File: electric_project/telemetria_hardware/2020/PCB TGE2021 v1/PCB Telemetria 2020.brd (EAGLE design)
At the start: 160 x 100 mm, 23 parts, among them IC1 INA240A1DR, IC2 MCP3221A6T-E_OTVAO, IC3 AZ1117IH-3.3TRG1, IC4 ACS758LCB-050B-PFF-T, J1 74655095R, J2 74655095R

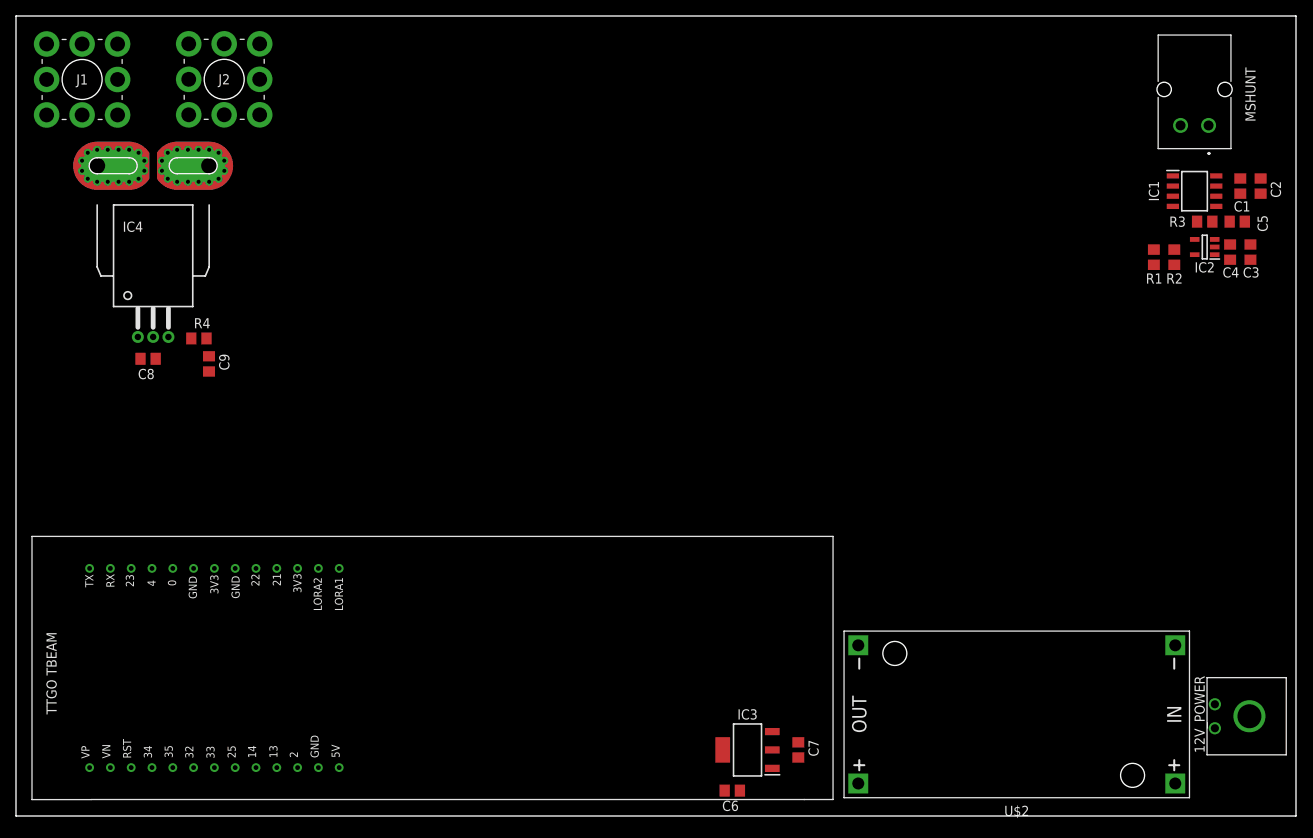
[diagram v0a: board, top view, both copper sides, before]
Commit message: Adding Current Input Traces an planes.
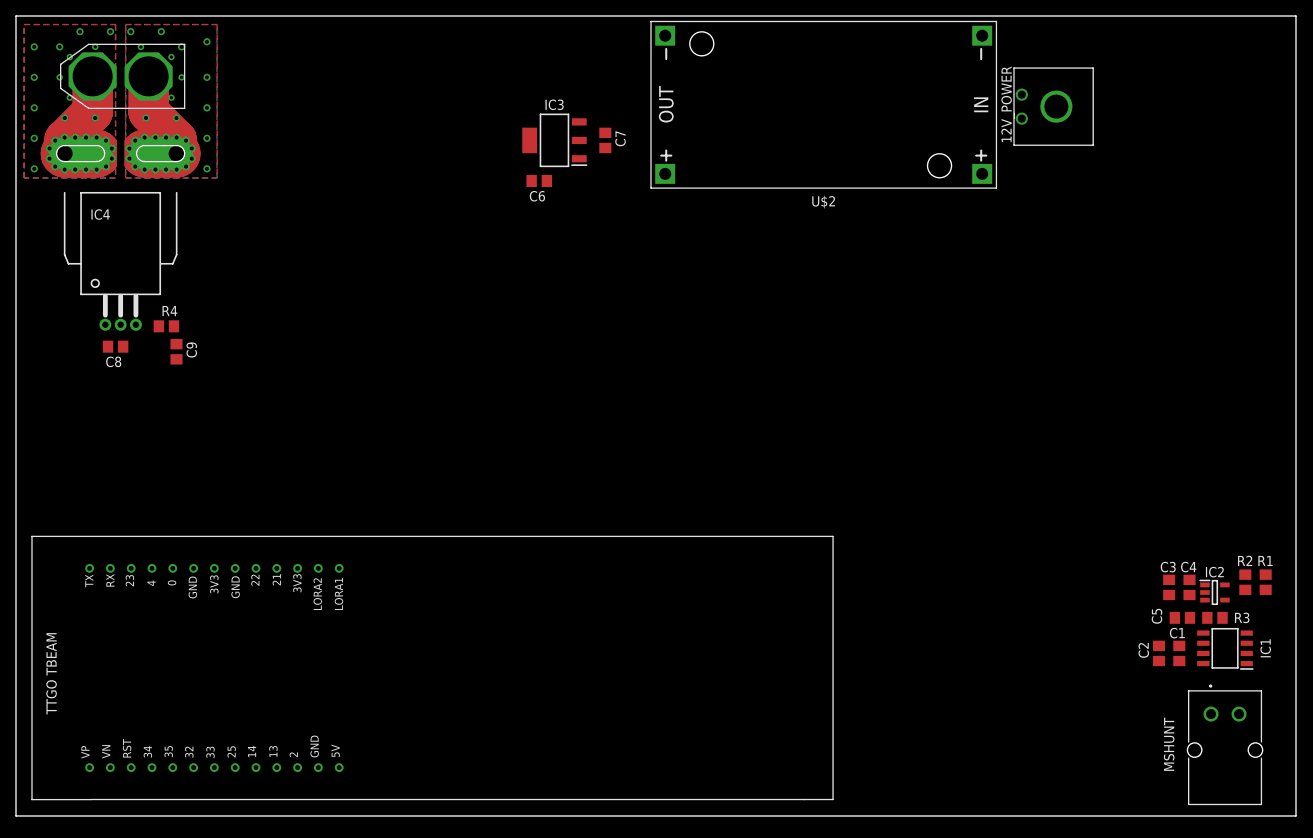
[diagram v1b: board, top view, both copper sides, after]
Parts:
- removed J1, J2: 74655095R, SamacSys_Parts:74655095R
- added U$3: XT60, XT60:XT60
- moved MSHUNT 81.4 mm to (151.1, 8.89), turned to 0 degrees
- moved 12V_POWER 79.9 mm to (125.7, 90.2)
- moved C6 79.9 mm to (65.4, 79.4)
- moved C7 79.9 mm to (73.7, 84.5)
- moved IC3 79.9 mm to (67.3, 84.5)
- moved U$2 79.9 mm to (101.0, 88.9)
- moved C2 59.8 mm to (142.9, 20.3), turned to 270 degrees
- moved C1 58.9 mm to (145.4, 20.3), turned to 270 degrees
- moved IC1 57.3 mm to (151.1, 21.0), turned to 180 degrees
- moved C5 50.0 mm to (145.8, 24.8), turned to 180 degrees
- moved R3 49.5 mm to (149.9, 24.8), turned to 0 degrees
- moved IC2 43.2 mm to (149.9, 27.9), turned to 0 degrees
- moved C3 43.1 mm to (144.1, 28.6), turned to 270 degrees
- moved R1 43.0 mm to (156.2, 29.2), turned to 90 degrees
- moved C4 42.2 mm to (146.7, 28.6), turned to 270 degrees
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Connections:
- net CMPPT_M: now also U$3.-; no longer J1.1, J1.2, J1.3, J1.4, J1.5, J1.6, J1.7, J1.8
- net CMPPT_P: now also U$3.+; no longer J2.1, J2.2, J2.3, J2.4, J2.5, J2.6, J2.7, J2.8
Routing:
- net CMPPT_M: track 0.00 -> 11.1 mm, vias 0 -> 14
- net CMPPT_P: track 0.00 -> 11.1 mm, vias 0 -> 14
- added copper zone on layer 1, net CMPPT_M
- added copper zone on layer 16, net CMPPT_M
- added copper zone on layer 1, net CMPPT_P
- added copper zone on layer 16, net CMPPT_P

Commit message: Position updates to the board.
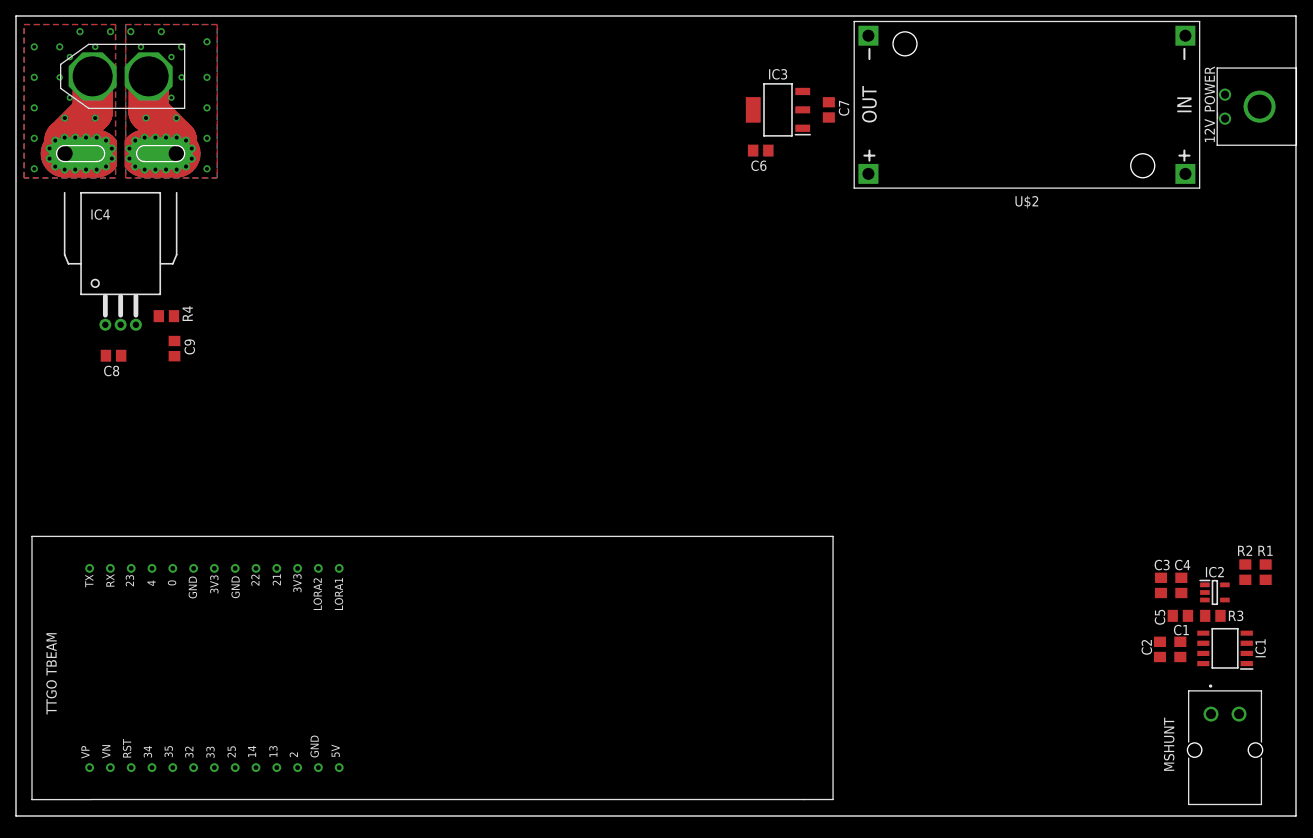
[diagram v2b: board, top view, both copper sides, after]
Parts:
- moved C7 28.2 mm to (101.6, 88.3)
- moved IC3 28.2 mm to (95.2, 88.3)
- moved C6 27.9 mm to (93.1, 83.2)
- moved 12V_POWER 25.4 mm to (151.1, 90.2)
- moved U$2 25.4 mm to (126.4, 88.9)
- moved R4 1.27 mm to (18.8, 62.5)
- moved R1 1.27 mm to (156.2, 30.5)
- moved R2 1.27 mm to (153.7, 30.5)
- moved C8 1.17 mm to (12.2, 57.5)
- moved C3 1.05 mm to (143.1, 28.8)
- moved C4 1.05 mm to (145.7, 28.8)
- moved C1 0.52 mm to (145.5, 20.8)
- moved C2 0.52 mm to (143.0, 20.8)
- moved C9 0.46 mm to (19.8, 58.4)
- moved R3 0.36 mm to (149.6, 25.0)
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
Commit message: just moved the LDO (not importante by now)
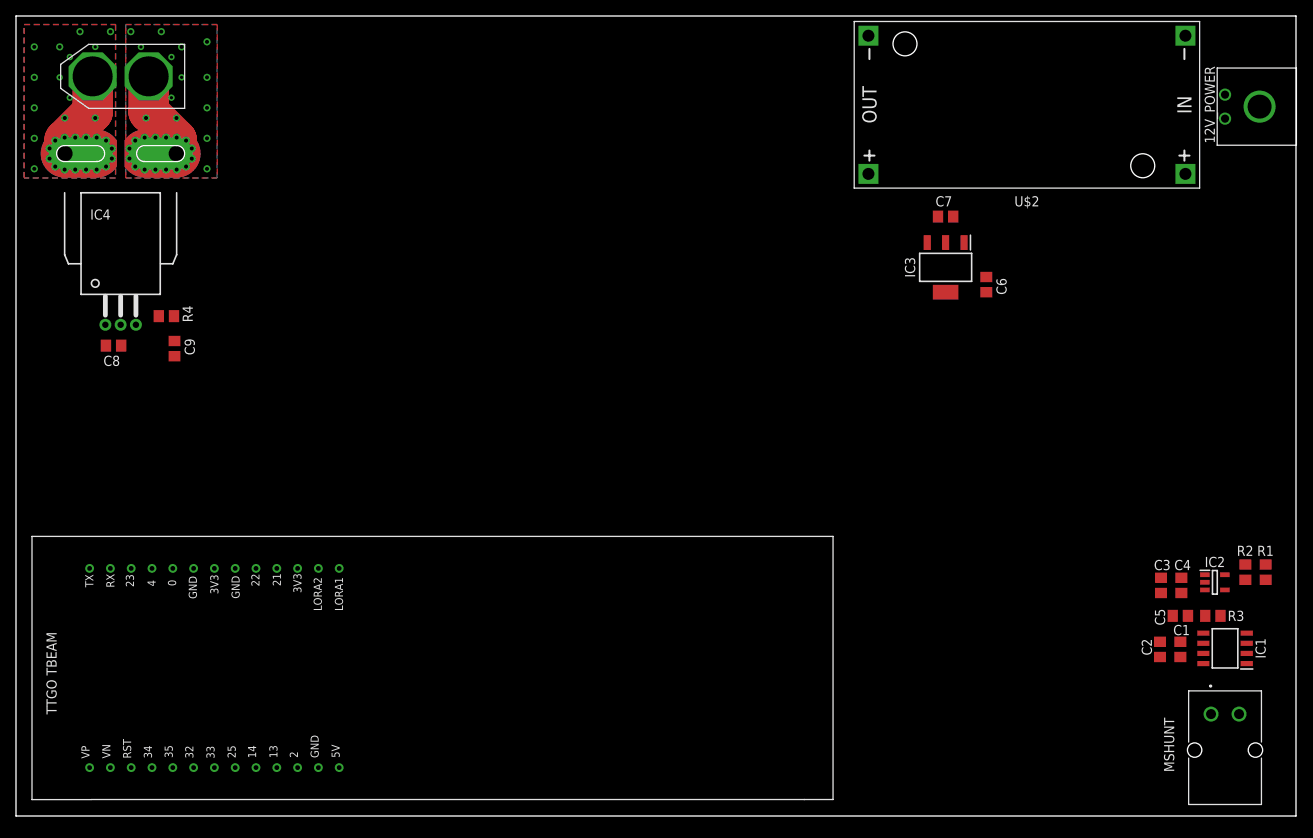
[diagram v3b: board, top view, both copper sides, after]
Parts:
- moved C6 32.8 mm to (121.3, 66.4), turned to 90 degrees
- moved IC3 28.8 mm to (116.2, 68.6), turned to 270 degrees
- moved C7 19.8 mm to (116.2, 74.9), turned to 0 degrees
- moved C8 1.27 mm to (12.2, 58.8)
- moved IC2 1.27 mm to (149.9, 29.2)

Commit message: Adding ADS1115 and BBank input circuit
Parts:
- added BBANK: 53259-0229, CON_MOLEX_53259-0229:0532590229
- added C10: 100nF, rcl:C0805
- added C11: 1nF, rcl:C0805
- added IC5: ADS1115IDGSR, SamacSys_Parts:SOP50P490X110-10N
- added R5: 220k, rcl:R0805
- added R6: 13.3k, rcl:R0805
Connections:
- new net AIN1: IC5.5
- new net AIN2: IC5.6
- new net AIN3: IC5.7
- new net BBANK_AIN0: C11.1, IC5.4, R5.2, R6.1
- new net VCC_BBANK: BBANK.1, R5.1
- net GND: now also BBANK.2, C10.2, C11.2, IC5.1, IC5.3, R6.2
- net I2C_SCL: now also IC5.10
- net I2C_SDA: now also IC5.9
- net VCC_3V3: now also C10.1, IC5.8

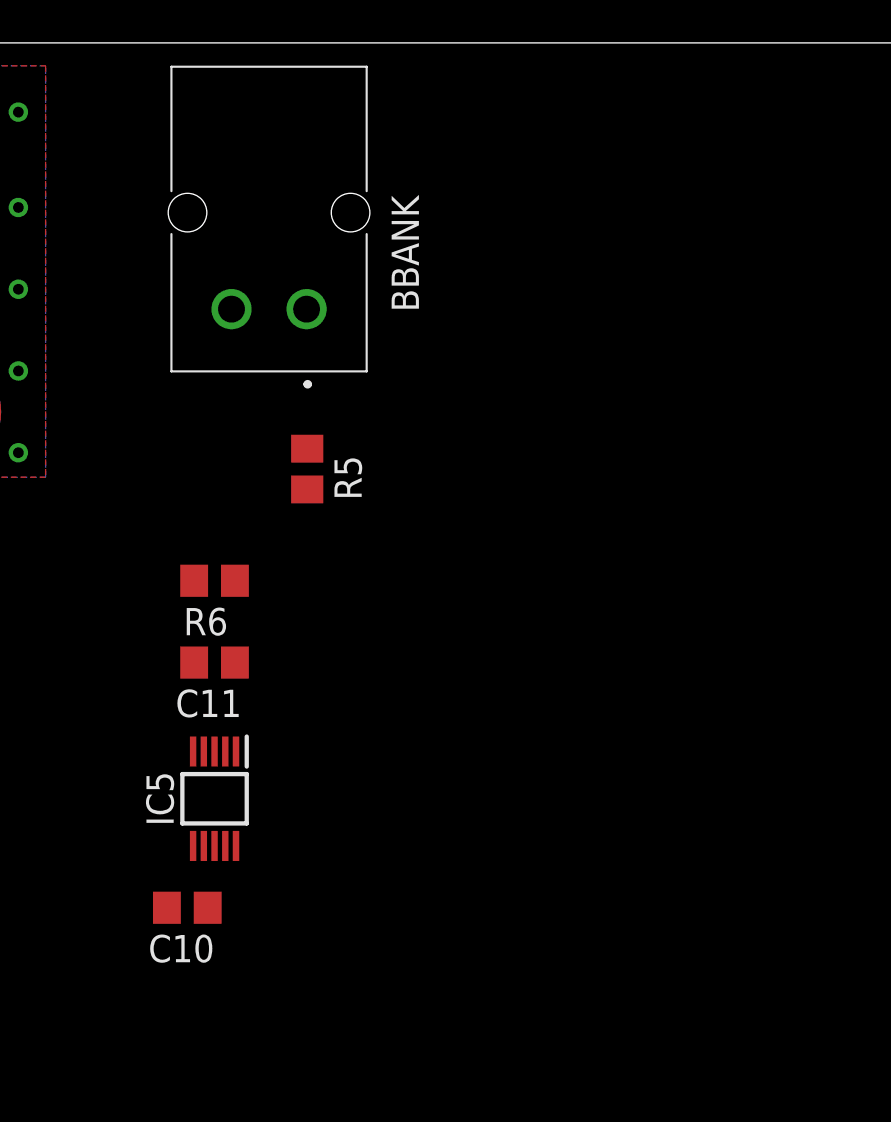
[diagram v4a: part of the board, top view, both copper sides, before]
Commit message: Adding the initial sch. of the PV voltage measurement circuit
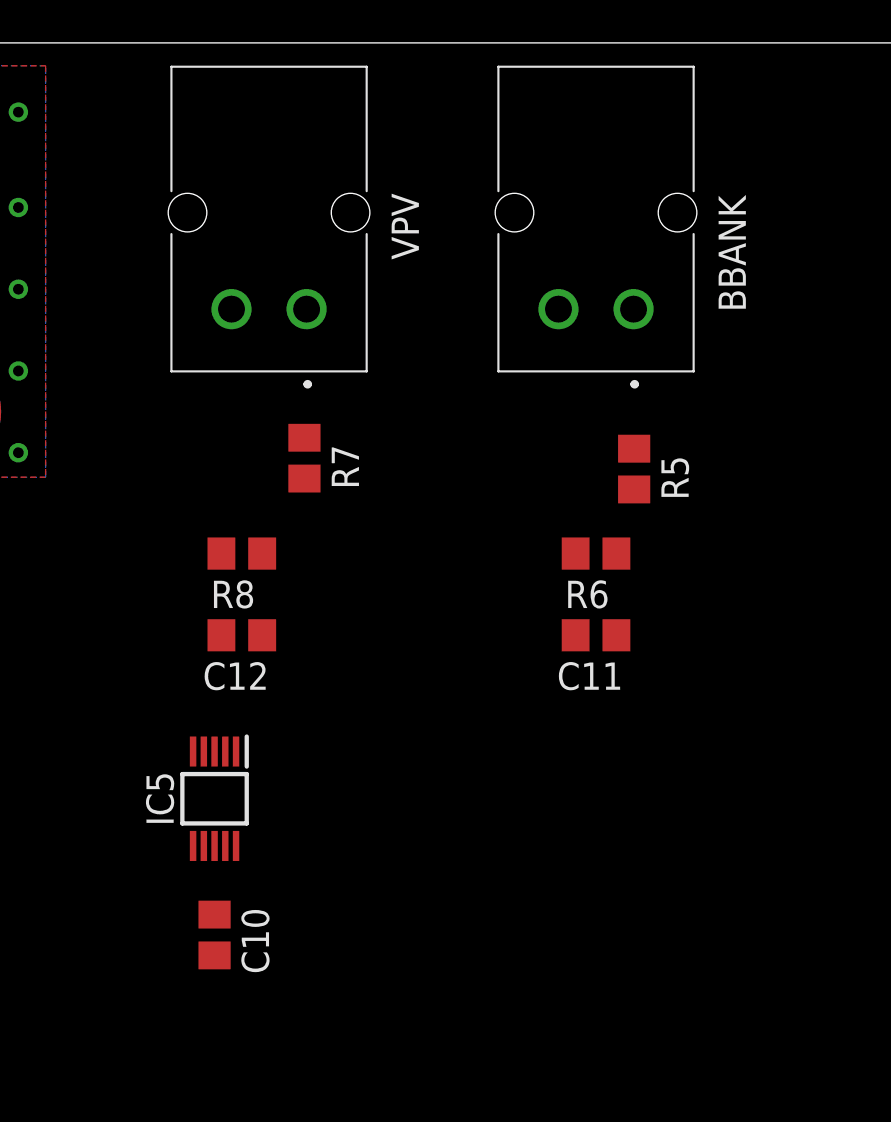
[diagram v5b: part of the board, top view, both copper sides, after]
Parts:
- added C12: (no value), rcl:C0805
- added R7, R8: (no value), rcl:R0805
- added VPV: 53259-0229, CON_MOLEX_53259-0229:0532590229
- moved C11 17.8 mm to (50.8, 72.4)
- moved R6 17.8 mm to (50.8, 76.2)
- moved R5 15.2 mm to (52.6, 80.1)
- moved BBANK 15.2 mm to (50.8, 91.4)
- moved C10 1.80 mm to (33.0, 58.4), turned to 270 degrees
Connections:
- removed net AIN1: IC5.5
- new net PV_AIN1: C12.1, IC5.5, R7.2, R8.1
- new net VCC_PV: R7.1, VPV.1
- net GND: now also C12.2, R8.2, VPV.2
